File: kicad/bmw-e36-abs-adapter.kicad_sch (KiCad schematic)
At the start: 40 parts

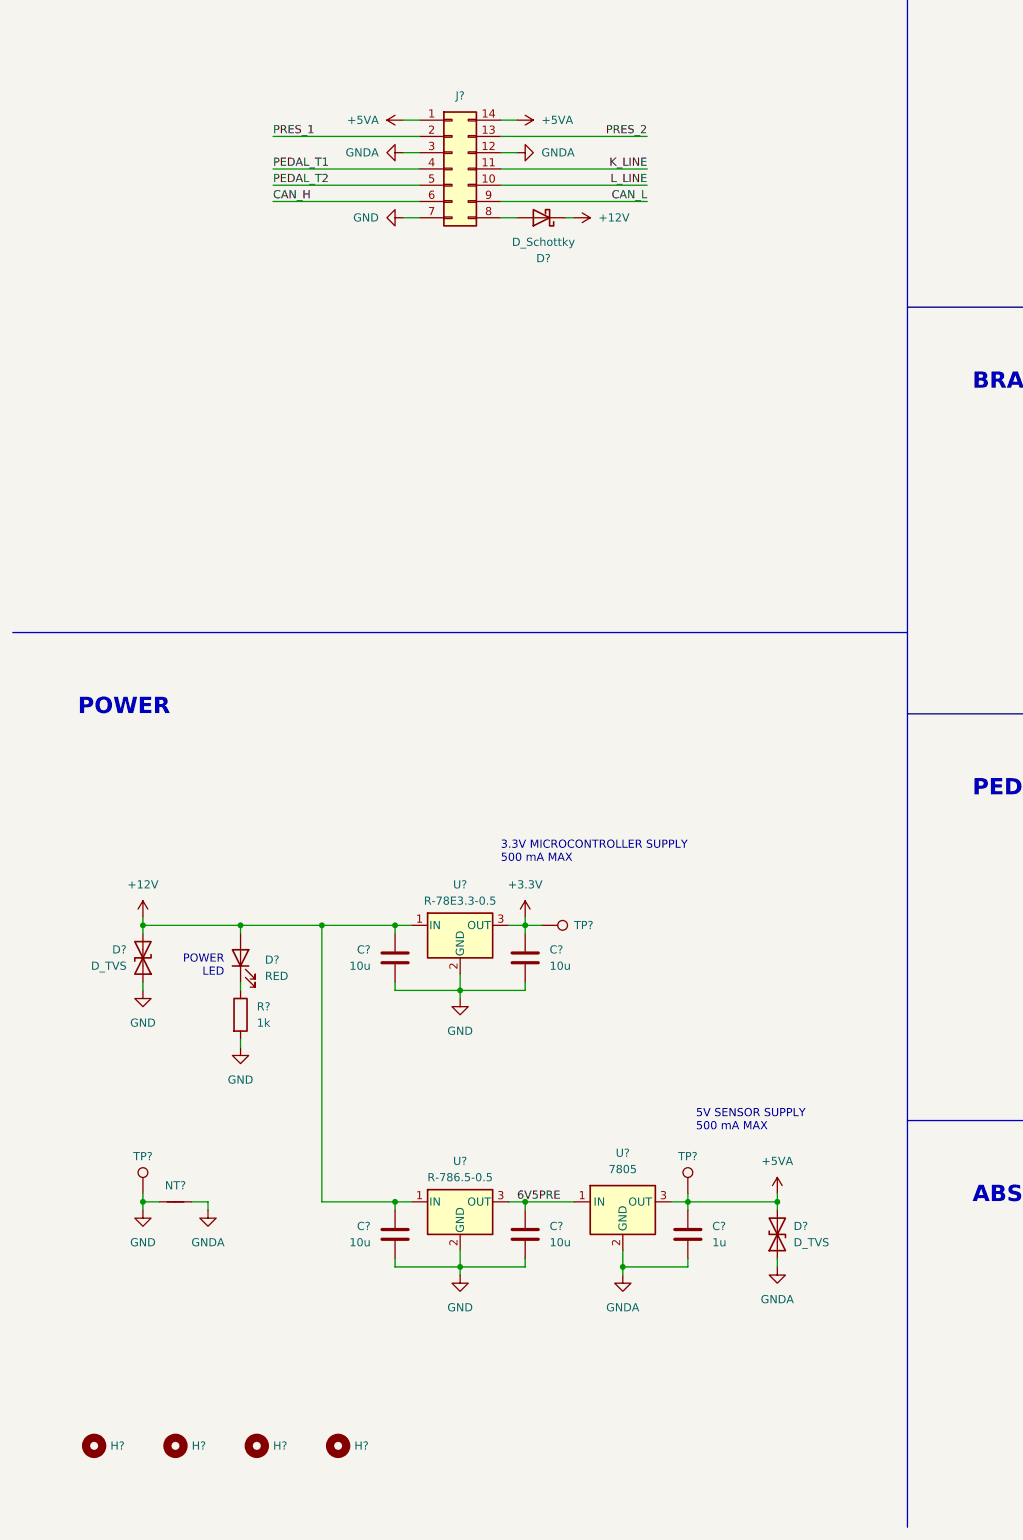
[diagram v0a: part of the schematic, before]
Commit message: Update power architecture and input protection
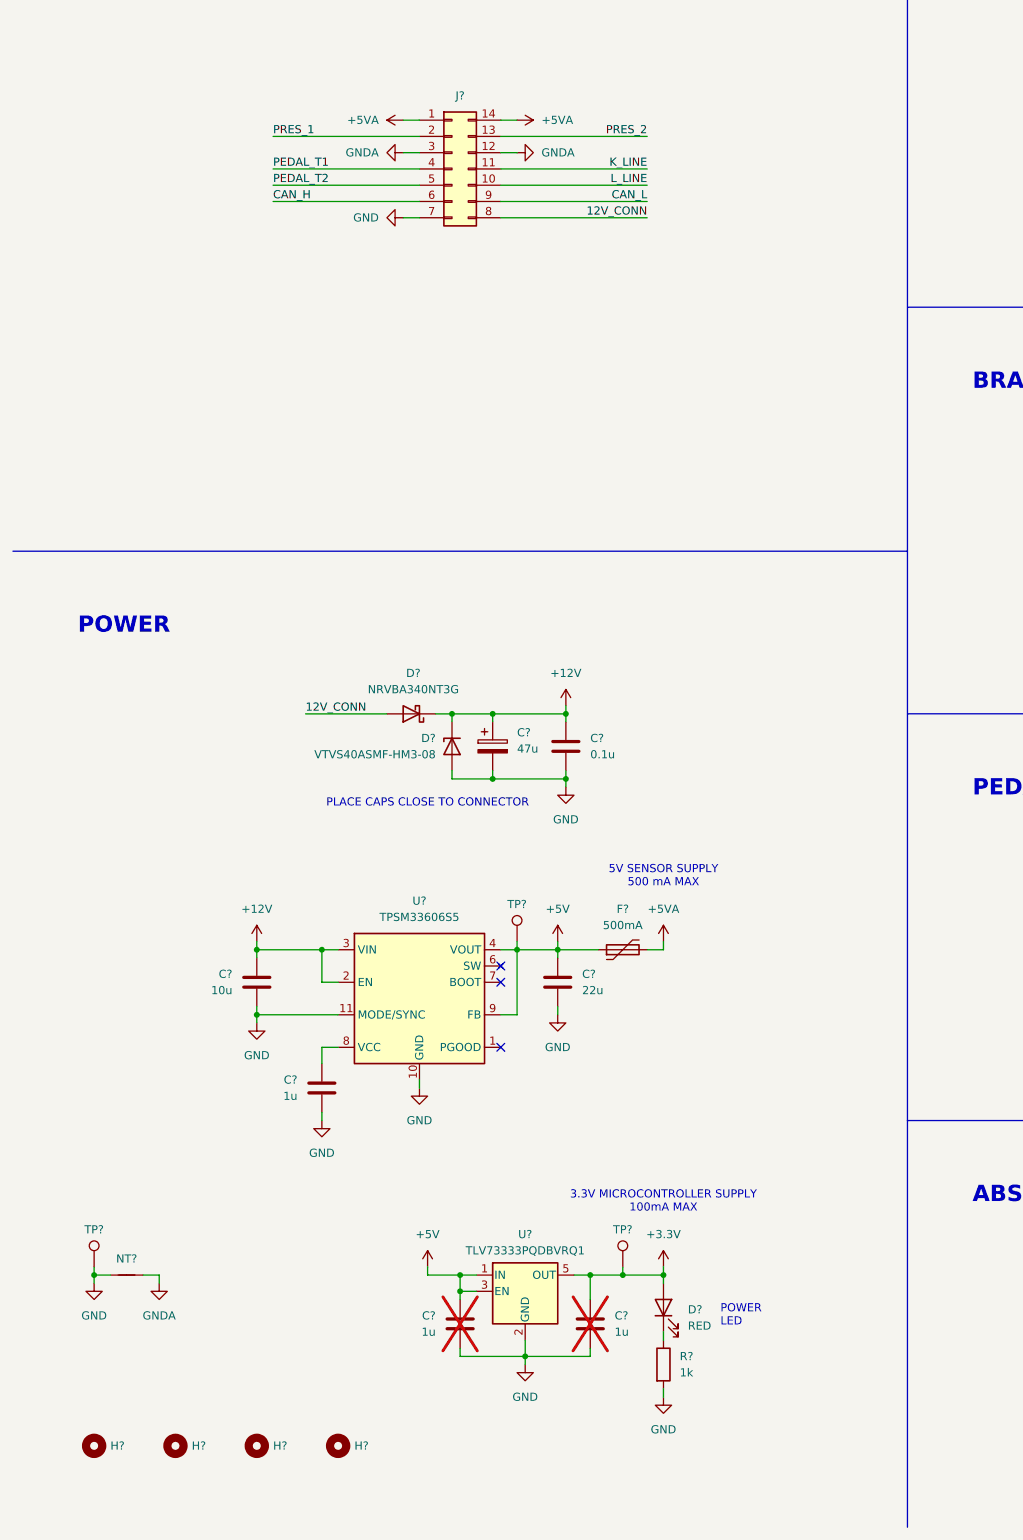
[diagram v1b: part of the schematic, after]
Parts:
- removed C? (x4): 10u, symbol symbols:C
- removed D?: D_TVS, symbol bmw-e36-abs-module:D_TVS
- removed D?: D_TVS, symbol symbols:D_TVS
- removed TP?: TestPoint, symbol symbols:TestPoint
- removed U?: R-78E3.3-0.5, Converter_DCDC:Converter_DCDC_RECOM_R-78E-0.5_THT, symbol symbols:R-78E3.3-0.5
- removed U?: R-786.5-0.5, Converter_DCDC:Converter_DCDC_RECOM_R-78E-0.5_THT, symbol symbols:R-786.5-0.5
- removed U?: 7805, Package_TO_SOT_SMD:SOT-223-3_TabPin2, symbol symbols:UA78M05QDCYRQ1
- added C?: 47u, Capacitor_SMD:CP_Elec_8x6.5, symbol symbols:C_Polarized
- added C? (x2): 1u, symbol symbols:C
- added C?: 10u, symbol symbols:C
- added C?: 0.1u, symbol symbols:C
- added C?: 22u, symbol symbols:C
- added D?: VTVS40ASMF-HM3-08, Diode_SMD:D_SMF, symbol symbols:D_Zener
- added F?: 500mA, Fuse:Fuse_1206_3216Metric, symbol symbols:Polyfuse
- added TP?: TestPoint, symbol symbols:TestPoint
- added U?: TPSM33606S5, symbol bmw-e36-abs-adapter:TPSM33606S5
- added U?: TLV73333PQDBVRQ1, Package_TO_SOT_SMD:SOT-23-5, symbol symbols:TLV73333PDBV
- C?: now not fitted
- D?: value D_Schottky -> NRVBA340NT3G; footprint (none) -> Diode_SMD:D_SMA; Manufacturer (none) -> onsemi; Part Number (none) -> NRVBA340NT3G
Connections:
- net +12V: now also C?.1, C?.1, C?.1, D?.1 (K), U?.2 (EN), U?.3 (VIN); no longer D?.2 (A)
- net +3.3V: now also D?.2 (A), C?.1, TP?.1, U?.5 (OUT)
- net +5VA: now also F?.2; no longer C?.1, TP?.1
- net GND: now also C?.2, C?.2, C?.2, C?.2, C?.2, C?.2, C?.2, D?.2 (A), U?.10 (GND), U?.11 (MODE/SYNC), U?.2 (GND)
- net GNDA: no longer C?.2
- net 12V_CONN: now reaches D?.2 (A), J?.8 (Pin_8)
- new net: C?.1, U?.8 (VCC)
- new net: U?.5 (SW), U?.6 (SW)
- new net +5V: C?.1, C?.1, F?.1, TP?.1, U?.1 (IN), U?.3 (EN), U?.4 (VOUT), U?.9 (FB)
- no-connect marks 9 -> 12
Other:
- note added: "3.3V MICROCONTROLLER SUPPLY 100mA MAX"
- note added: "PLACE CAPS CLOSE TO CONNECTOR"
- note removed: "3.3V MICROCONTROLLER SUPPLY 500 mA MAX"
- moved on the sheet: D?, NT?, R?, TP?

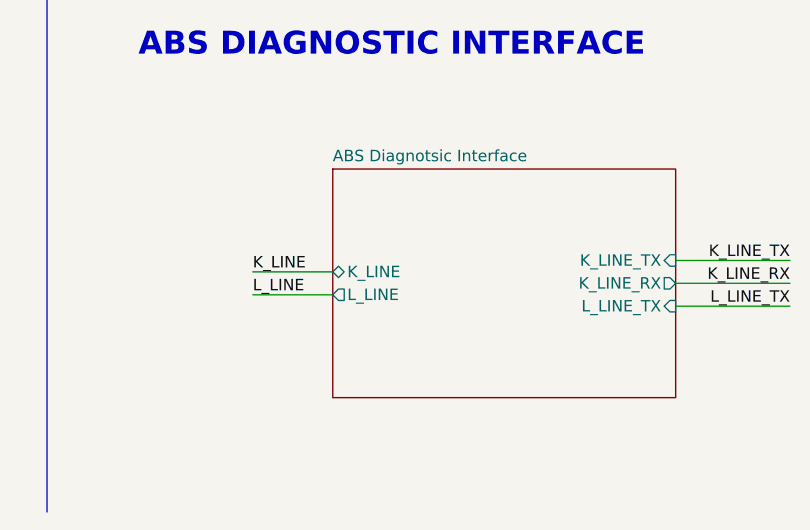
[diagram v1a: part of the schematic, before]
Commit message: Update ABS diagnostic interface
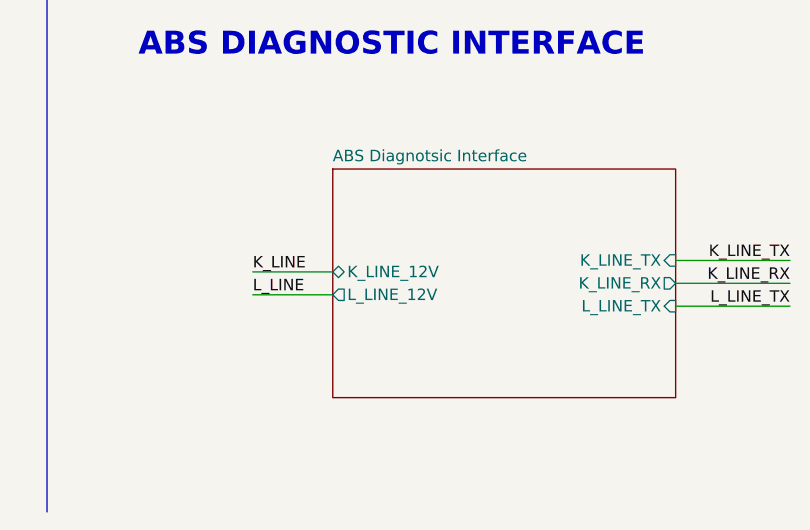
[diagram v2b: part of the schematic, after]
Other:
- sheet ABS Diagnotsic Interface ports: added K_LINE_12V, L_LINE_12V; removed K_LINE, L_LINE
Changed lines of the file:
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@@
 			)
 		)
-		(pin "K_LINE" bidirectional
+		(pin "K_LINE_12V" bidirectional
 			(at 184.15 240.03 180)
 			(effects
@@
 			)
 		)
-		(pin "L_LINE" output
+		(pin "L_LINE_12V" output
 			(at 184.15 242.57 180)
 			(effects

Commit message: Update connector; annotate and assign footprints
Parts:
- removed J?: Conn_02x07_Counter_Clockwise, symbol symbols:Conn_02x07_Counter_Clockwise
- added J1: TE_9-6437287-8, bmw-e36-abs-adapter:TE_9-6437287-8, symbol bmw-e36-abs-adapter:TE_9-6437287-8
- C1, C5: renamed from C?; footprint (none) -> Capacitor_SMD:C_1206_3216Metric
- C10, C8: renamed from C?; value 4.7u -> 10u; footprint (none) -> Capacitor_SMD:C_1206_3216Metric
- C11, C12, C13, C14, C15, C16, C2, C3, C6, C7, C9: renamed from C?; footprint (none) -> Capacitor_SMD:C_0603_1608Metric
- D3, D4: renamed from D?; footprint (none) -> LED_SMD:LED_0603_1608Metric
- H1, H2, H3, H4: renamed from H?; footprint (none) -> MountingHole:MountingHole_3.2mm_M3
- J2: renamed from J?; footprint (none) -> Connector:Tag-Connect_TC2030-IDC-NL_2x03_P1.27mm_Vertical
- JP1: renamed from JP?; value Jumper_2_Open -> RST; footprint (none) -> Jumper:SolderJumper-2_P1.3mm_Open_RoundedPad1.0x1.5mm
- JP2: renamed from JP?; value Jumper_2_Open -> BOOT; footprint (none) -> Jumper:SolderJumper-2_P1.3mm_Open_RoundedPad1.0x1.5mm
- NT1: renamed from NT?; footprint (none) -> NetTie:NetTie-2_SMD_Pad0.5mm
- R1, R2, R3, R4: renamed from R?; footprint (none) -> Resistor_SMD:R_0603_1608Metric
- TP1, TP2, TP3: renamed from TP?; footprint (none) -> TestPoint:TestPoint_Pad_D2.0mm
- gave numbers to parts that had none: 8
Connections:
- net +5VA: now also J1.18 (Pin_18), J1.19 (Pin_19)
- net 12V_CONN: now also J1.26 (Pin_26)
- net CAN_H: now also J1.20 (Pin_20)
- net CAN_L: now also J1.14 (Pin_14)
- net GND: now also J1.21 (Pin_21), J1.22 (Pin_22)
- net GNDA: now also J1.12 (Pin_12), J1.13 (Pin_13)
- net K_LINE: now also J1.3 (Pin_3)
- net L_LINE: now also J1.4 (Pin_4)
- net PEDAL_T1: now also J1.1 (Pin_1)
- net PEDAL_T2: now also J1.2 (Pin_2)
- net PRES_1: now also J1.7 (Pin_7)
- net PRES_2: now also J1.6 (Pin_6)
- no-connect marks 12 -> 23
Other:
- note added: "1"
- note added: "13"
- note added: "14"
- note added: "19"
- note added: "20"
- note added: "26"
- note added: "7"
- note added: "8"
- note added: "AMP 9-6437287-8"
- note added: "MATING CONN: 3-1437290-7 TERMINALS: 3-1447221-3 (18-22 AWG) CAVITY PLUG: 4-1437284-3"
- note added: "PLACE CLOSE TO PINS VDD: 1uu & 0.1u VDDA: 1u & 0.01u VDDIO2: 1uu & 0.1u"
- note removed: "PLACE CLOSE TO PINS VDD: 4.7u & 0.1u VDDA: 1u & 0.01u VDDIO2: 4.u & 0.1u"

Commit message: Update footprints
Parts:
- U1: footprint (none) -> bmw-e36-abs-adapter:Texas_RDN0011B_QFN-FCMOD-11-3.5x4.5mm-P0.5mm_2EP
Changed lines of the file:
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@@
 			)
 		)
-		(property "Footprint" ""
+		(property "Footprint" "bmw-e36-abs-adapter:Texas_RDN0011B_QFN-FCMOD-11-3.5x4.5mm-P0.5mm_2EP"
 			(at 76.2 184.15 0)
 			(hide yes)

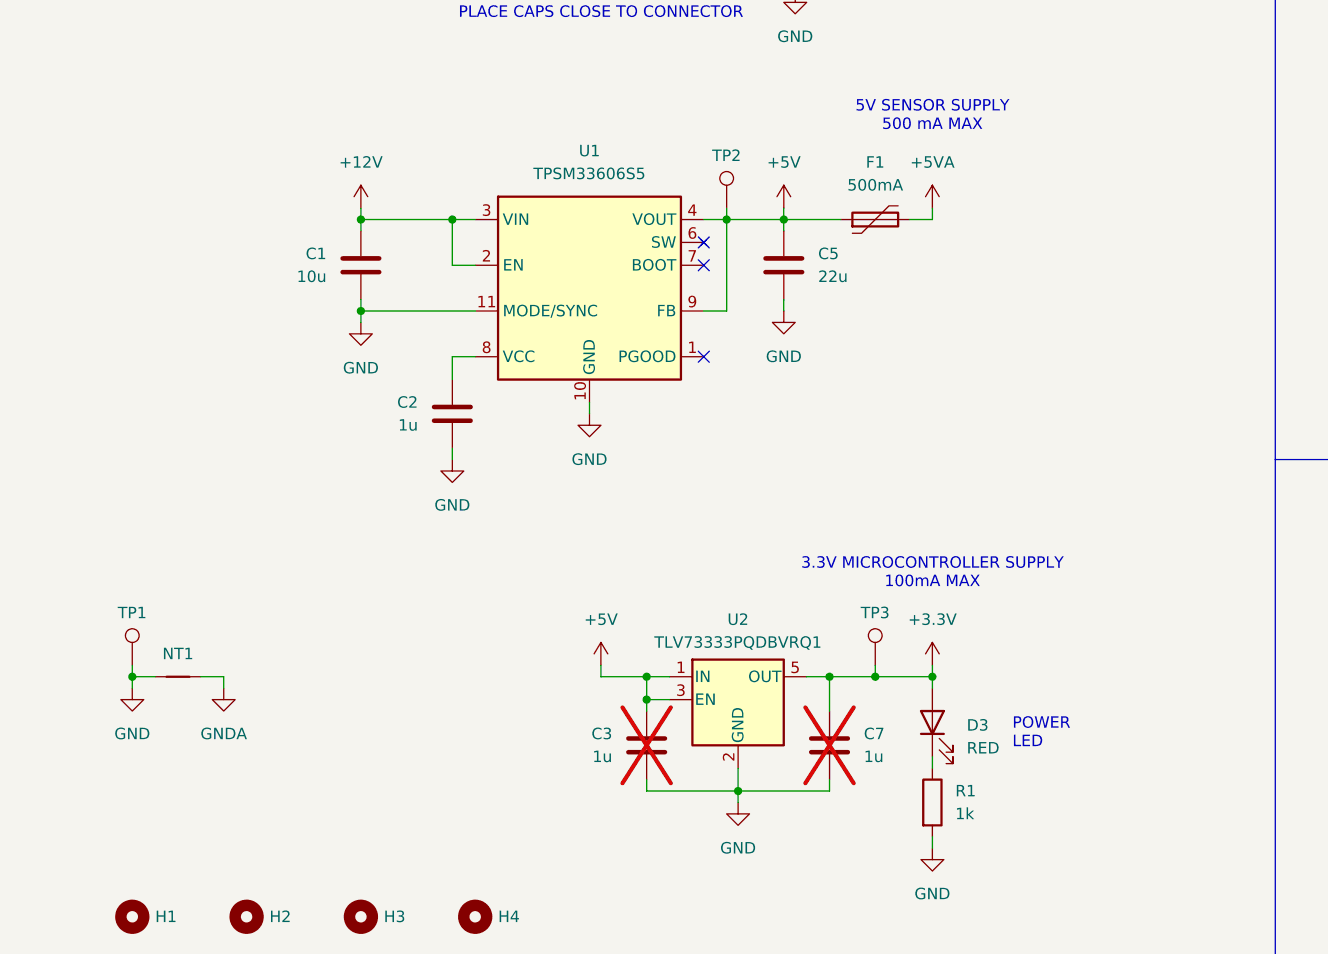
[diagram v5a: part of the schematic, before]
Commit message: Update part numbers and fix ERC issues
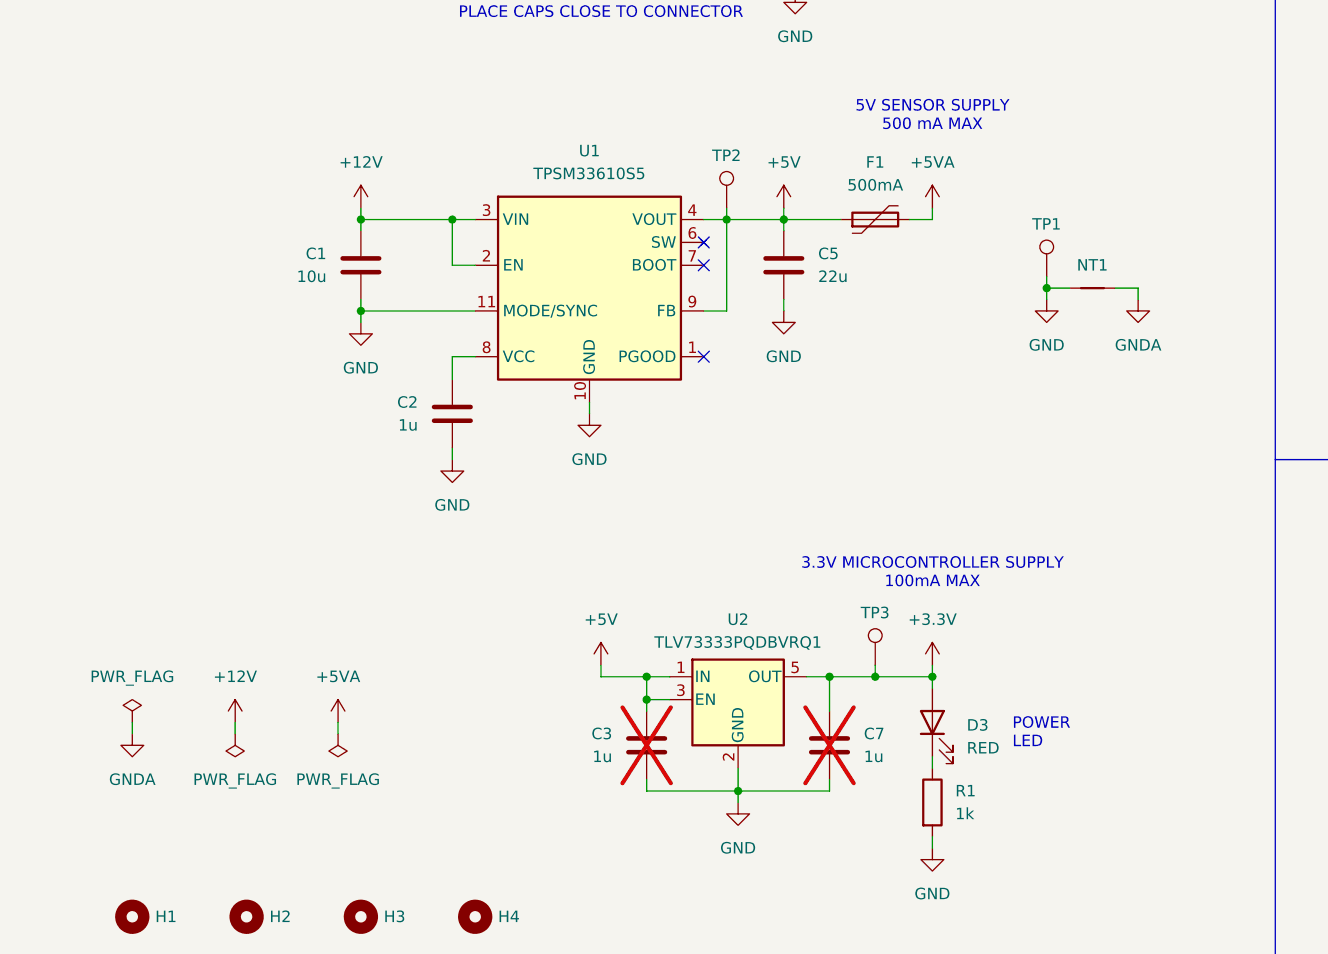
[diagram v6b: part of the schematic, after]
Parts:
- C1, C10, C8: Manufacturer (none) -> Murata; Part Number (none) -> GRT31CR61H106KE01L
- C11, C13, C6, C9: Manufacturer (none) -> Murata; Part Number (none) -> GCJ188R71H104KA12D
- C12, C14: Manufacturer (none) -> Murata; Part Number (none) -> GCM1885C2A120JA16D
- C15, C2: Manufacturer (none) -> Murata; Part Number (none) -> GRT188R71E105KE13D
- C16: Manufacturer (none) -> Murata; Part Number (none) -> GCM188R71H103KA37D
- C3, C7: Manufacturer (none) -> Murata; Part Number (none) -> GRT188R71E105KE13D; now left out of the parts list
- C5: Manufacturer (none) -> Murata; Part Number (none) -> GRT31CC81C226KE01L
- D1: symbol bmw-e36-abs-module:D_Schottky -> symbols:D_Schottky
- D3: symbol bmw-e36-abs-module:LED -> symbols:LED; Manufacturer (none) -> Rohm; Part Number (none) -> SML-D12V8WT86C
- D4: symbol bmw-e36-abs-module:LED -> symbols:LED; Manufacturer (none) -> Rohm; Part Number (none) -> SML-D12P8WT86C
- H1, H2, H3, H4: symbol bmw-e36-abs-module:MountingHole -> symbols:MountingHole
- J1: Manufacturer (none) -> TE AMP; Part Number (none) -> 9-6437287-8
- J2, JP1, JP2, TP1, TP2, TP3: now left out of the parts list
- R1, R4: Manufacturer (none) -> Panasonic; Part Number (none) -> ERJ-3EKF1001V
- R2, R3: Manufacturer (none) -> Panasonic; Part Number (none) -> ERJ-3EKF22R0V
- U1: value TPSM33606S5 -> TPSM33610S5; Manufacturer (none) -> Texas Instruments; Part Number (none) -> TPSM33610S5QRDNRQ1
- U3: Manufacturer (none) -> ST; Part Number (none) -> STM32F042K6U6
- Y1: Manufacturer (none) -> ECS; Part Number (none) -> ECS-160-10-36Q-AES-TR
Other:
- moved on the sheet: NT1, TP1
